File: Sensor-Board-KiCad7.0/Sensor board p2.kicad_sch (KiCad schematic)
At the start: 61 parts, among them J10 9401-0-15-15-23-27-10-0, J11 9401-0-15-15-23-27-10-0, J12 9401-0-15-15-23-27-10-0, J13 9401-0-15-15-23-27-10-0, J14 9401-0-15-15-23-27-10-0, J15 9401-0-15-15-23-27-10-0, J16 9401-0-15-15-23-27-10-0, J17 9401-0-15-15-23-27-10-0, J18 9401-0-15-15-23-27-10-0, U11 OPA396DCKT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

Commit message: Made pin changes to EChem sensors
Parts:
- J10, J11, J12, J13, J14, J15, J16, J17, J18: footprint EChem socket:CONN_0384-0-67-80-23-27-10-0_MIM -> CONN_0384-0-67-80-23-27-10-0_MIM
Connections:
- net Count2_CO: now also J13.1; no longer J13.
- net Count2_NO2: now also J10.1; no longer J10.
- net Count2_SO2: now also J16.1; no longer J16.
- net Ref2_CO: now also J15.1; no longer J15.
- net Ref2_NO2: now also J12.1; no longer J12.
- net Ref2_SO2: now also J18.1; no longer J18.
- net Sens2_CO: now also J14.1; no longer J14.
- net Sens2_NO2: now also J11.1; no longer J11.
- net Sens2_SO2: now also J17.1; no longer J17.

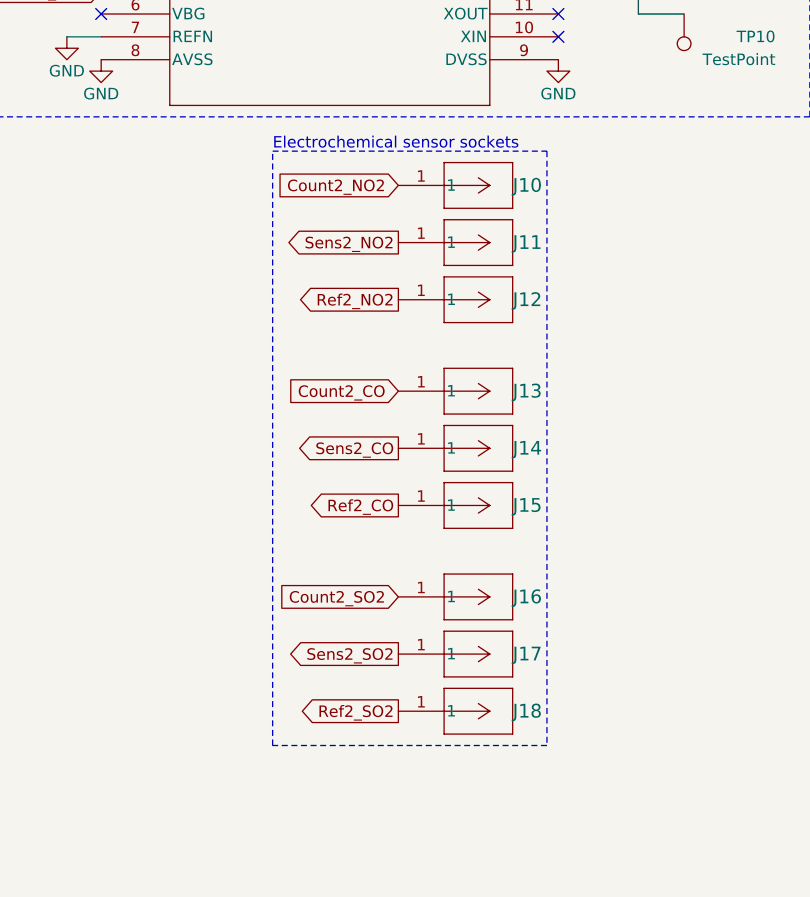
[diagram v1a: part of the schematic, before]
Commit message: Added footprints for components
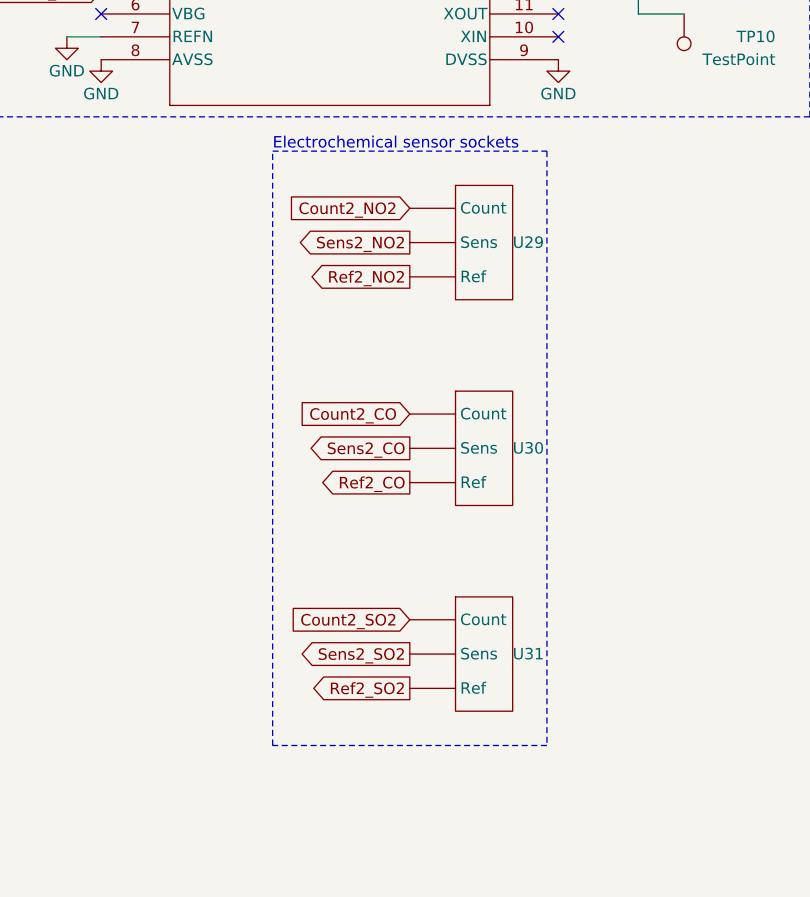
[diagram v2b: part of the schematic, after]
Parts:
- removed J10, J11, J12, J13, J14, J15, J16, J17, J18: 9401-0-15-15-23-27-10-0, CONN_0384-0-67-80-23-27-10-0_MIM, symbol EChem socket:9401-0-15-15-23-27-10-0
- added U29, U30, U31: ~, EChem socket:3-pin socket, symbol EChem socket:3-pin_socket
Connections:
- net Count2_CO: now also U30. (Sens)
- net Count2_NO2: now also U29. (Sens)
- net Count2_SO2: now also U31. (Sens)
- net Ref2_CO: now also U30. (Sens)
- net Ref2_NO2: now also U29. (Sens)
- net Ref2_SO2: now also U31. (Sens)
- net Sens2_CO: now also U30. (Sens)
- net Sens2_NO2: now also U29. (Sens)
- net Sens2_SO2: now also U31. (Sens)

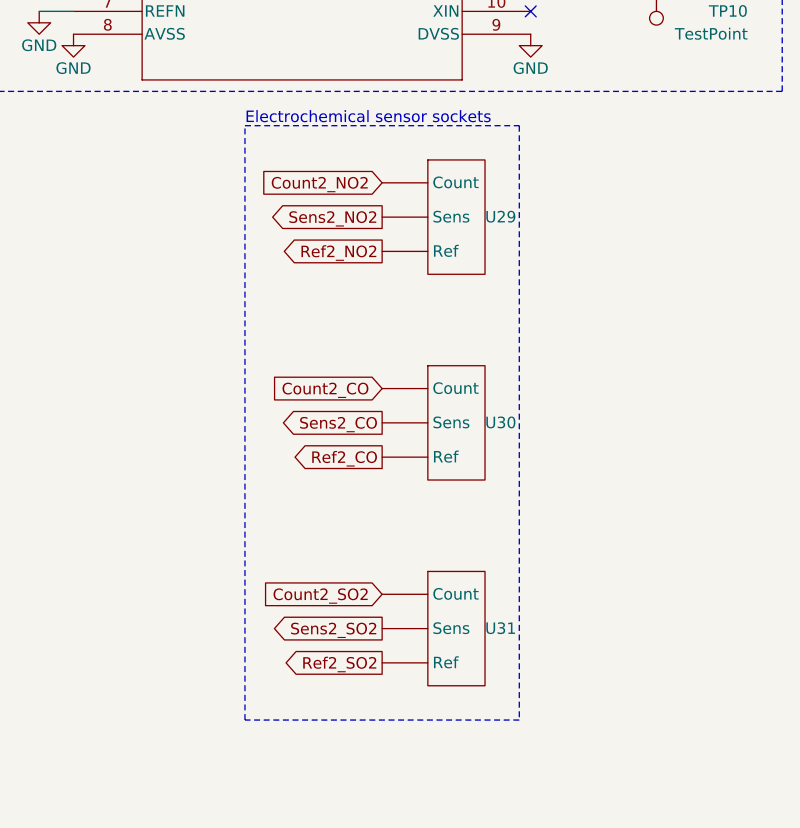
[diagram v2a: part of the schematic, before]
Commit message: Fixed I2C Connector pin numbers
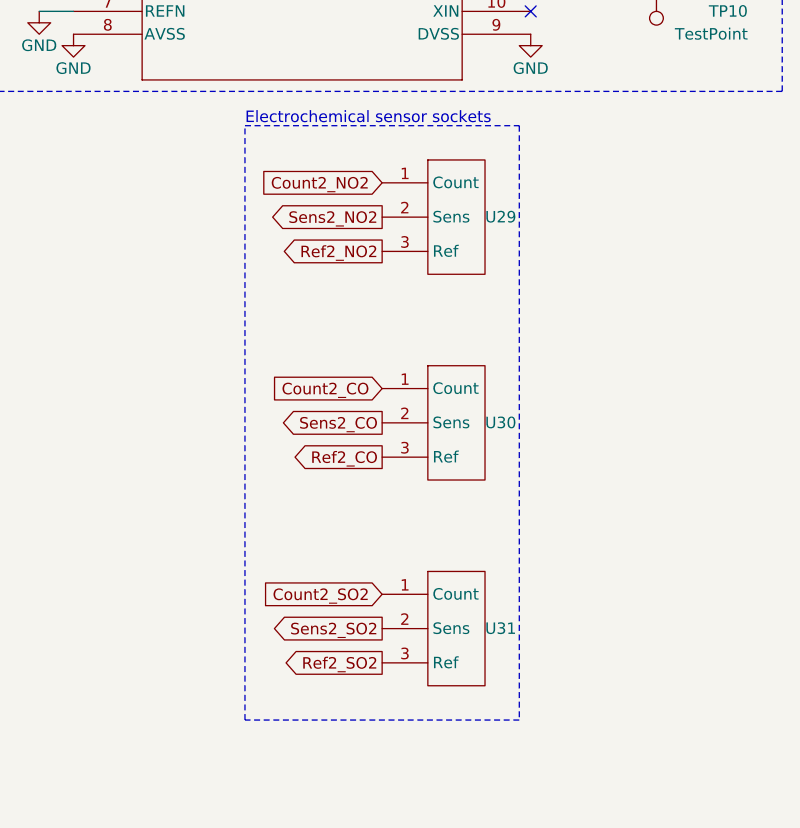
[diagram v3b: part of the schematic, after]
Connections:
- net Count2_CO: now also U30.1 (Count); no longer U30. (Sens)
- net Count2_NO2: now also U29.1 (Count); no longer U29. (Sens)
- net Count2_SO2: now also U31.1 (Count); no longer U31. (Sens)
- net Ref2_CO: now also U30.3 (Ref); no longer U30. (Sens)
- net Ref2_NO2: now also U29.3 (Ref); no longer U29. (Sens)
- net Ref2_SO2: now also U31.3 (Ref); no longer U31. (Sens)
- net Sens2_CO: now also U30.2 (Sens); no longer U30. (Sens)
- net Sens2_NO2: now also U29.2 (Sens); no longer U29. (Sens)
- net Sens2_SO2: now also U31.2 (Sens); no longer U31. (Sens)
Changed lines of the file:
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@@
-    )
-  )
-  (symbol (lib_id "EChem socket:3-pin_socket") (at 241.3 137.16 0) (unit 1)
-    (in_bom yes) (on_board yes) (dnp no)
-    (property "Reference" "U30" (at 247.65 130.81 0)
-      (effects (font (size 1.27 1.27)) (justify left))
-    )
-    (property "Value" "~" (at 241.3 137.16 0)
-      (effects (font (size 1.27 1.27)))
-    )
-    (property "Footprint" "EChem socket:3-pin socket" (at 241.3 137.16 0)
-      (effects (font (size 1.27 1.27)) hide)
-    )
-    (property "Datasheet" "" (at 241.3 137.16 0)
-      (effects (font (size 1.27 1.27)) hide)
-    )
-    (pin "")
-    (pin "")
-    (pin "")
-    (instances
-      (project "Sensor-Board"
-        (path "/3a986dcd-349f-492d-950a-09832b2e5abd/eb03ba60-66c2-4345-a3c2-908f0a643e89"
-          (reference "U30") (unit 1)
-        )
-      )
     )
   )
@@
     )
   )
-  (symbol (lib_id "EChem socket:3-pin_socket") (at 241.3 160.02 0) (unit 1)
-    (in_bom yes) (on_board yes) (dnp no)
-    (property "Reference" "U31" (at 247.65 153.67 0)
-      (effects (font (size 1.27 1.27)) (justify left))
-    )
-    (property "Value" "~" (at 241.3 160.02 0)
-      (effects (font (size 1.27 1.27)))
-    )
-    (property "Footprint" "EChem socket:3-pin socket" (at 241.3 160.02 0)
-      (effects (font (size 1.27 1.27)) hide)
-    )
-    (property "Datasheet" "" (at 241.3 160.02 0)
-      (effects (font (size 1.27 1.27)) hide)
-    )
-    (pin "")
-    (pin "")
-    (pin "")
-    (instances
-      (project "Sensor-Board"
-        (path "/3a986dcd-349f-492d-950a-09832b2e5abd/eb03ba60-66c2-4345-a3c2-908f0a643e89"
-          (reference "U31") (unit 1)
-        )
-      )
-    )
-  )
   (symbol (lib_name "GND_5") (lib_id "power:GND") (at 34.29 48.26 0) (unit 1)
     (in_bom yes) (on_board yes) (dnp no) (fields_autoplaced)
@@
         (path "/3a986dcd-349f-492d-950a-09832b2e5abd/eb03ba60-66c2-4345-a3c2-908f0a643e89"
           (reference "R45") (unit 1)
-        )
-      )
-    )
-  )
-  (symbol (lib_id "EChem socket:3-pin_socket") (at 241.3 114.3 0) (unit 1)
-    (in_bom yes) (on_board yes) (dnp no)
-    (property "Reference" "U29" (at 247.65 107.95 0)
-      (effects (font (size 1.27 1.27)) (justify left))
-    )
-    (property "Value" "~" (at 241.3 114.3 0)
-      (effects (font (size 1.27 1.27)))
-    )
-    (property "Footprint" "EChem socket:3-pin socket" (at 241.3 114.3 0)
-      (effects (font (size 1.27 1.27)) hide)
-    )
-    (property "Datasheet" "" (at 241.3 114.3 0)
-      (effects (font (size 1.27 1.27)) hide)
-    )
-    (pin "")
-    (pin "")
-    (pin "")
-    (instances
-      (project "Sensor-Board"
-        (path "/3a986dcd-349f-492d-950a-09832b2e5abd/eb03ba60-66c2-4345-a3c2-908f0a643e89"
-          (reference "U29") (unit 1)
         )
       )
@@
     )
   )
+  (symbol (lib_id "EChem socket:3-pin_socket") (at 241.3 160.02 0) (unit 1)
+    (in_bom yes) (on_board yes) (dnp no)
+    (property "Reference" "U31" (at 247.65 153.67 0)
+      (effects (font (size 1.27 1.27)) (justify left))
+    )
+    (property "Value" "~" (at 241.3 160.02 0)
+      (effects (font (size 1.27 1.27)))
+    )
+    (property "Footprint" "EChem socket:3-pin socket" (at 241.3 160.02 0)
+      (effects (font (size 1.27 1.27)) hide)
+    )
+    (property "Datasheet" "" (at 241.3 160.02 0)
+      (effects (font (size 1.27 1.27)) hide)
+    )
+    (pin "2")
+    (pin "1")
+    (pin "3")
+    (instances
+      (project "Sensor-Board"
+        (path "/3a986dcd-349f-492d-950a-09832b2e5abd/eb03ba60-66c2-4345-a3c2-908f0a643e89"
+          (reference "U31") (unit 1)
+        )
+      )
+    )
+  )
   (symbol (lib_id "Device:C") (at 63.5 24.13 270) (unit 1)
     (in_bom yes) (on_board yes) (dnp no) (fields_autoplaced)
@@
     )
   )
+  (symbol (lib_id "EChem socket:3-pin_socket") (at 241.3 137.16 0) (unit 1)
+    (in_bom yes) (on_board yes) (dnp no)
+    (property "Reference" "U30" (at 247.65 130.81 0)
+      (effects (font (size 1.27 1.27)) (justify left))
+    )
+    (property "Value" "~" (at 241.3 137.16 0)
+      (effects (font (size 1.27 1.27)))
+    )
+    (property "Footprint" "EChem socket:3-pin socket" (at 241.3 137.16 0)
+      (effects (font (size 1.27 1.27)) hide)
+    )
+    (property "Datasheet" "" (at 241.3 137.16 0)
+      (effects (font (size 1.27 1.27)) hide)
+    )
+    (pin "2")
+    (pin "1")
+    (pin "3")
+    (instances
+      (project "Sensor-Board"
+        (path "/3a986dcd-349f-492d-950a-09832b2e5abd/eb03ba60-66c2-4345-a3c2-908f0a643e89"
+          (reference "U30") (unit 1)
+        )
+      )
+    )
+  )
   (symbol (lib_id "power:+3.3V") (at 161.29 154.94 270) (unit 1)
     (in_bom yes) (on_board yes) (dnp no)
@@
         )
       )
+    )
+  )
+  (symbol (lib_id "EChem socket:3-pin_socket") (at 241.3 114.3 0) (unit 1)
+    (in_bom yes) (on_board yes) (dnp no)
+    (property "Reference" "U29" (at 247.65 107.95 0)
+      (effects (font (size 1.27 1.27)) (justify left))
+    )
+    (property "Value" "~" (at 241.3 114.3 0)
+      (effects (font (size 1.27 1.27)))
+    )
+    (property "Footprint" "EChem socket:3-pin socket" (at 241.3 114.3 0)
+      (effects (font (size 1.27 1.27)) hide)
+    )
+    (property "Datasheet" "" (at 241.3 114.3 0)
+      (effects (font (size 1.27 1.27)) hide)
+    )
+    (pin "2")
+    (pin "1")
+    (pin "3")
+    (instances
+      (project "Sensor-Board"
+        (path "/3a986dcd-349f-492d-950a-09832b2e5abd/eb03ba60-66c2-4345-a3c2-908f0a643e89"
+          (reference "U29") (unit 1)
+        )
+      )

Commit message: Fixed prelim layout errors and started traces
Fixed pad sizes for EChem sensor footprint.
Fixed silkscreen warnings.
Started routing traces in layout.
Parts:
- U29, U30, U31: footprint EChem socket:3-pin socket -> (none)

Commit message: Moved components around
Moved resistors and test points around. Continued trying to route vias along the board.
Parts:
- U29, U30, U31: footprint (none) -> EChem socket:3-pin socket
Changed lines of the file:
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@@
-    )
-  )
-  (symbol (lib_id "EChem socket:3-pin_socket") (at 241.3 160.02 0) (unit 1)
-    (in_bom yes) (on_board yes) (dnp no)
-    (property "Reference" "U31" (at 247.65 153.67 0)
-      (effects (font (size 1.27 1.27)) (justify left))
-    )
-    (property "Value" "~" (at 241.3 160.02 0)
-      (effects (font (size 1.27 1.27)))
-    )
-    (property "Footprint" "" (at 241.3 160.02 0)
-      (effects (font (size 1.27 1.27)) hide)
-    )
-    (property "Datasheet" "" (at 241.3 160.02 0)
-      (effects (font (size 1.27 1.27)) hide)
-    )
-    (pin "3")
-    (pin "1")
-    (pin "2")
-    (instances
-      (project "Sensor-Board"
-        (path "/3a986dcd-349f-492d-950a-09832b2e5abd/eb03ba60-66c2-4345-a3c2-908f0a643e89"
-          (reference "U31") (unit 1)
-        )
-      )
     )
   )
@@
     )
   )
+  (symbol (lib_id "EChem socket:3-pin_socket") (at 241.3 114.3 0) (unit 1)
+    (in_bom yes) (on_board yes) (dnp no)
+    (property "Reference" "U29" (at 247.65 107.95 0)
+      (effects (font (size 1.27 1.27)) (justify left))
+    )
+    (property "Value" "~" (at 241.3 114.3 0)
+      (effects (font (size 1.27 1.27)))
+    )
+    (property "Footprint" "EChem socket:3-pin socket" (at 241.3 114.3 0)
+      (effects (font (size 1.27 1.27)) hide)
+    )
+    (property "Datasheet" "" (at 241.3 114.3 0)
+      (effects (font (size 1.27 1.27)) hide)
+    )
+    (pin "3")
+    (pin "1")
+    (pin "2")
+    (instances
+      (project "Sensor-Board"
+        (path "/3a986dcd-349f-492d-950a-09832b2e5abd/eb03ba60-66c2-4345-a3c2-908f0a643e89"
+          (reference "U29") (unit 1)
+        )
+      )
+    )
+  )
   (symbol (lib_id "Connector:TestPoint") (at 252.73 29.21 0) (unit 1)
     (in_bom yes) (on_board yes) (dnp no)
@@
         (path "/3a986dcd-349f-492d-950a-09832b2e5abd/eb03ba60-66c2-4345-a3c2-908f0a643e89"
           (reference "#PWR080") (unit 1)
-        )
-      )
-    )
-  )
-  (symbol (lib_id "EChem socket:3-pin_socket") (at 241.3 114.3 0) (unit 1)
-    (in_bom yes) (on_board yes) (dnp no)
-    (property "Reference" "U29" (at 247.65 107.95 0)
-      (effects (font (size 1.27 1.27)) (justify left))
-    )
-    (property "Value" "~" (at 241.3 114.3 0)
-      (effects (font (size 1.27 1.27)))
-    )
-    (property "Footprint" "" (at 241.3 114.3 0)
-      (effects (font (size 1.27 1.27)) hide)
-    )
-    (property "Datasheet" "" (at 241.3 114.3 0)
-      (effects (font (size 1.27 1.27)) hide)
-    )
-    (pin "3")
-    (pin "1")
-    (pin "2")
-    (instances
-      (project "Sensor-Board"
-        (path "/3a986dcd-349f-492d-950a-09832b2e5abd/eb03ba60-66c2-4345-a3c2-908f0a643e89"
-          (reference "U29") (unit 1)
         )
       )
@@
       (effects (font (size 1.27 1.27)))
     )
-    (property "Footprint" "" (at 241.3 137.16 0)
+    (property "Footprint" "EChem socket:3-pin socket" (at 241.3 137.16 0)
       (effects (font (size 1.27 1.27)) hide)
     )
@@
         )
       )
+    )
+  )
+  (symbol (lib_id "EChem socket:3-pin_socket") (at 241.3 160.02 0) (unit 1)
+    (in_bom yes) (on_board yes) (dnp no)
+    (property "Reference" "U31" (at 247.65 153.67 0)
+      (effects (font (size 1.27 1.27)) (justify left))
+    )
+    (property "Value" "~" (at 241.3 160.02 0)
+      (effects (font (size 1.27 1.27)))
+    )
+    (property "Footprint" "EChem socket:3-pin socket" (at 241.3 160.02 0)
+      (effects (font (size 1.27 1.27)) hide)
+    )
+    (property "Datasheet" "" (at 241.3 160.02 0)
+      (effects (font (size 1.27 1.27)) hide)
+    )
+    (pin "3")
+    (pin "1")
+    (pin "2")
+    (instances
+      (project "Sensor-Board"
+        (path "/3a986dcd-349f-492d-950a-09832b2e5abd/eb03ba60-66c2-4345-a3c2-908f0a643e89"
+          (reference "U31") (unit 1)
+        )
+      )
